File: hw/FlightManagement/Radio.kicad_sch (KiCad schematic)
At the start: 41 parts, among them J1 BWSMA-KE-Z001, U6 XA17-G4K, Y1 13.56 MHz, Y2 10.7 MHz, Y3 6.6128 MHz

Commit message: add pdf outputs
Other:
- company: (none) -> Daniel Enrique Pérez Díaz (steewBSD)
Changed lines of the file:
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@@
 	(generator_version "9.0")
 	(paper "A4")
+	(title_block
+		(company "Daniel Enrique Pérez Díaz (steewBSD)")
+	)
 	(text_box "Receiver\n(433 MHz Vertical)"
 		(exclude_from_sim no)

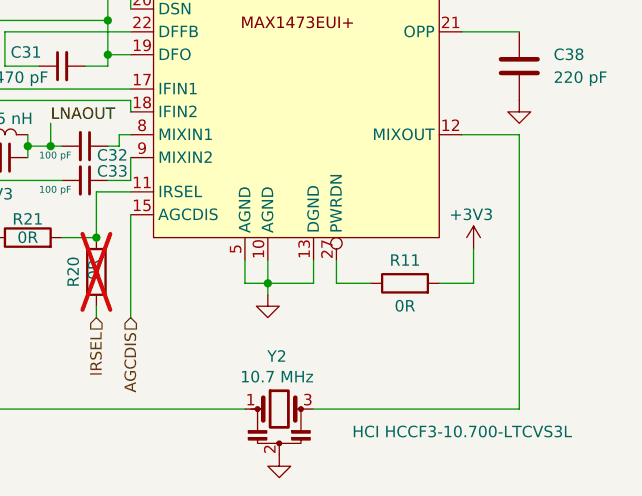
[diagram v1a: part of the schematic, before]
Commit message: add NOR flash in FC
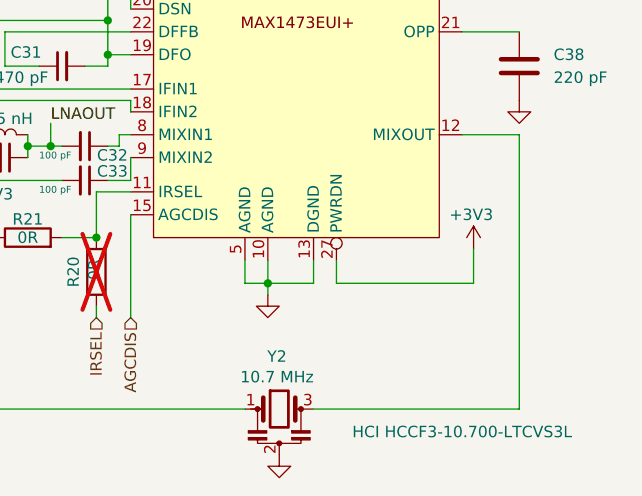
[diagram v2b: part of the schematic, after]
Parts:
- removed R11: 0R, Resistor_SMD:R_0603_1608Metric_Pad0.98x0.95mm_HandSolder, symbol Device:R
- C17, C18, C19, C20, C21, C22, C23, C24, C25, C26, C27, C28, C29, C30, C31, C32, C33, C34, C35, C36, C37, C38, C47: footprint Capacitor_SMD:C_0805_2012Metric_Pad1.18x1.45mm_HandSolder -> Capacitor_SMD:C_0603_1608Metric_Pad1.08x0.95mm_HandSolder
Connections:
- net +3V3: now also U7.27 (PWRDN)
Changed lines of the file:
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@@
 	(wire
 		(pts
-			(xy 226.06 119.38) (xy 222.25 119.38)
-		)
-		(stroke
-			(width 0)
-			(type default)
-		)
-	)
-	(wire
-		(pts
 			(xy 185.42 86.36) (xy 185.42 90.17)
 		)
@@
 	(wire
 		(pts
-			(xy 210.82 119.38) (xy 214.63 119.38)
+			(xy 210.82 119.38) (xy 226.06 119.38)
 		)
 		(stroke
@@
 			)
 		)
-		(property "Footprint" "Capacitor_SMD:C_0805_2012Metric_Pad1.18x1.45mm_HandSolder"
+		(property "Footprint" "Capacitor_SMD:C_0603_1608Metric_Pad1.08x0.95mm_HandSolder"
 			(at 167.64 80.01 0)
 			(effects
@@
 			)
 		)
-		(property "Footprint" "Capacitor_SMD:C_0805_2012Metric_Pad1.18x1.45mm_HandSolder"
+		(property "Footprint" "Capacitor_SMD:C_0603_1608Metric_Pad1.08x0.95mm_HandSolder"
 			(at 232.1052 99.06 0)
 			(effects
@@
 			)
 		)
-		(property "Footprint" "Capacitor_SMD:C_0805_2012Metric_Pad1.18x1.45mm_HandSolder"
+		(property "Footprint" "Capacitor_SMD:C_0603_1608Metric_Pad1.08x0.95mm_HandSolder"
 			(at 106.68 73.66 0)
 			(effects
@@
 	)
 	(symbol
-		(lib_id "Device:R")
-		(at 218.44 119.38 90)
-		(unit 1)
-		(exclude_from_sim no)
-		(in_bom yes)
-		(on_board yes)
-		(dnp no)
-		(property "Reference" "R11"
-			(at 218.44 116.84 90)
-			(effects
-				(font
-					(size 1.27 1.27)
-				)
-			)
-		)
-		(property "Value" "0R"
-			(at 218.44 121.92 90)
-			(effects
-				(font
-					(size 1.27 1.27)
-				)
-			)
-		)
-		(property "Footprint" "Resistor_SMD:R_0603_1608Metric_Pad0.98x0.95mm_HandSolder"
-			(at 218.44 121.158 90)
-			(effects
-				(font
-					(size 1.27 1.27)
-				)
-				(hide yes)
-			)
-		)
-		(property "Datasheet" "~"
-			(at 218.44 119.38 0)
-			(effects
-				(font
-					(size 1.27 1.27)
-				)
-				(hide yes)
-			)
-		)
-		(property "Description" "Resistor"
-			(at 218.44 119.38 0)
-			(effects
-				(font
-					(size 1.27 1.27)
-				)
-				(hide yes)
-			)
-		)
-		(pin "2"
-		)
-		(pin "1"
-		)
-		(instances
-			(project "FlightManagement"
-				(path "/428dbf80-1251-4f56-8786-11b9f3c75d18/59439b12-3d5b-4d3f-87cb-66bd691f4bfb"
-					(reference "R11")
-					(unit 1)
-				)
-			)
-		)
-	)
-	(symbol
 		(lib_id "Device:C_Small")
 		(at 165.1 111.76 180)
@@
 			)
 		)
-		(property "Footprint" "Capacitor_SMD:C_0805_2012Metric_Pad1.18x1.45mm_HandSolder"
+		(property "Footprint" "Capacitor_SMD:C_0603_1608Metric_Pad1.08x0.95mm_HandSolder"
 			(at 165.1 111.76 0)
 			(effects
@@
 			)
 		)
-		(property "Footprint" "Capacitor_SMD:C_0805_2012Metric_Pad1.18x1.45mm_HandSolder"
+		(property "Footprint" "Capacitor_SMD:C_0603_1608Metric_Pad1.08x0.95mm_HandSolder"
 			(at 78.74 76.2 0)
 			(effects
@@
 			)
 		)
-		(property "Footprint" "Capacitor_SMD:C_0805_2012Metric_Pad1.18x1.45mm_HandSolder"
+		(property "Footprint" "Capacitor_SMD:C_0603_1608Metric_Pad1.08x0.95mm_HandSolder"
 			(at 154.94 64.77 0)
 			(effects
@@
 			)
 		)
-		(property "Footprint" "Capacitor_SMD:C_0805_2012Metric_Pad1.18x1.45mm_HandSolder"
+		(property "Footprint" "Capacitor_SMD:C_0603_1608Metric_Pad1.08x0.95mm_HandSolder"
 			(at 198.12 57.15 0)
 			(effects
@@
 			)
 		)
-		(property "Footprint" "Capacitor_SMD:C_0805_2012Metric_Pad1.18x1.45mm_HandSolder"
+		(property "Footprint" "Capacitor_SMD:C_0603_1608Metric_Pad1.08x0.95mm_HandSolder"
 			(at 125.73 62.23 0)
 			(effects
@@
 			)
 		)
-		(property "Footprint" "Capacitor_SMD:C_0805_2012Metric_Pad1.18x1.45mm_HandSolder"
+		(property "Footprint" "Capacitor_SMD:C_0603_1608Metric_Pad1.08x0.95mm_HandSolder"
 			(at 173.99 105.41 0)
 			(effects
@@
 			)
 		)
-		(property "Footprint" "Capacitor_SMD:C_0805_2012Metric_Pad1.18x1.45mm_HandSolder"
+		(property "Footprint" "Capacitor_SMD:C_0603_1608Metric_Pad1.08x0.95mm_HandSolder"
 			(at 124.46 86.36 0)
 			(effects
@@
 			)
 		)
-		(property "Footprint" "Capacitor_SMD:C_0805_2012Metric_Pad1.18x1.45mm_HandSolder"
+		(property "Footprint" "Capacitor_SMD:C_0603_1608Metric_Pad1.08x0.95mm_HandSolder"
 			(at 212.09 57.15 0)
 			(effects
@@
 			)
 		)
-		(property "Footprint" "Capacitor_SMD:C_0805_2012Metric_Pad1.18x1.45mm_HandSolder"
+		(property "Footprint" "Capacitor_SMD:C_0603_1608Metric_Pad1.08x0.95mm_HandSolder"
 			(at 217.17 57.15 0)
 			(effects
@@
 			)
 		)
-		(property "Footprint" "Capacitor_SMD:C_0805_2012Metric_Pad1.18x1.45mm_HandSolder"
+		(property "Footprint" "Capacitor_SMD:C_0603_1608Metric_Pad1.08x0.95mm_HandSolder"
 			(at 182.88 107.95 0)
 			(effects
@@
 			)
 		)
-		(property "Footprint" "Capacitor_SMD:C_0805_2012Metric_Pad1.18x1.45mm_HandSolder"
+		(property "Footprint" "Capacitor_SMD:C_0603_1608Metric_Pad1.08x0.95mm_HandSolder"
 			(at 182.88 104.14 0)
 			(effects
@@
 			)
 		)
-		(property "Footprint" "Capacitor_SMD:C_0805_2012Metric_Pad1.18x1.45mm_HandSolder"
+		(property "Footprint" "Capacitor_SMD:C_0603_1608Metric_Pad1.08x0.95mm_HandSolder"
 			(at 154.94 59.69 0)
 			(effects
@@
 			)
 		)
-		(property "Footprint" "Capacitor_SMD:C_0805_2012Metric_Pad1.18x1.45mm_HandSolder"
+		(property "Footprint" "Capacitor_SMD:C_0603_1608Metric_Pad1.08x0.95mm_HandSolder"
 			(at 205.74 57.15 0)
 			(effects
@@
 			)
 		)
-		(property "Footprint" "Capacitor_SMD:C_0805_2012Metric_Pad1.18x1.45mm_HandSolder"
+		(property "Footprint" "Capacitor_SMD:C_0603_1608Metric_Pad1.08x0.95mm_HandSolder"
 			(at 180.34 95.25 0)
 			(effects
@@
 			)
 		)
-		(property "Footprint" "Capacitor_SMD:C_0805_2012Metric_Pad1.18x1.45mm_HandSolder"
+		(property "Footprint" "Capacitor_SMD:C_0603_1608Metric_Pad1.08x0.95mm_HandSolder"
 			(at 109.22 86.36 0)
 			(effects
@@
 			)
 		)
-		(property "Footprint" "Capacitor_SMD:C_0805_2012Metric_Pad1.18x1.45mm_HandSolder"
+		(property "Footprint" "Capacitor_SMD:C_0603_1608Metric_Pad1.08x0.95mm_HandSolder"
 			(at 113.03 73.66 0)
 			(effects
@@
 			)
 		)
-		(property "Footprint" "Capacitor_SMD:C_0805_2012Metric_Pad1.18x1.45mm_HandSolder"
+		(property "Footprint" "Capacitor_SMD:C_0603_1608Metric_Pad1.08x0.95mm_HandSolder"
 			(at 100.33 73.66 0)
 			(effects
@@
 			)
 		)
-		(property "Footprint" "Capacitor_SMD:C_0805_2012Metric_Pad1.18x1.45mm_HandSolder"
+		(property "Footprint" "Capacitor_SMD:C_0603_1608Metric_Pad1.08x0.95mm_HandSolder"
 			(at 150.8252 109.22 0)
 			(effects
@@
 			)
 		)
-		(property "Footprint" "Capacitor_SMD:C_0805_2012Metric_Pad1.18x1.45mm_HandSolder"
+		(property "Footprint" "Capacitor_SMD:C_0603_1608Metric_Pad1.08x0.95mm_HandSolder"
 			(at 100.33 82.55 0)
 			(effects
@@
 			)
 		)
-		(property "Footprint" "Capacitor_SMD:C_0805_2012Metric_Pad1.18x1.45mm_HandSolder"
+		(property "Footprint" "Capacitor_SMD:C_0603_1608Metric_Pad1.08x0.95mm_HandSolder"
 			(at 155.9052 109.22 0)
 			(effects

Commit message: FMU completed
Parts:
- renumbered C22 to C14, C31 to C21, C33 to C23, C47 to C26, C37 to C27, C29 to C28, C23 to C29, C21 to C30, C18 to C31, C25 to C32, C24 to C33, C26 to C34, C38 to C35, C19 to C36, C17 to C37, C28 to C38, C36 to C39, C35 to C40, C34 to C41, C30 to C51, C32 to C52, C27 to C7, C20 to C9, J1 to J4, L1 to L3, L2 to L4, L4 to L5, L3 to L6, L5 to L7, R21 to R10, R20 to R14, R17 to R16, R16 to R17, R10 to R18, U6 to U5, U5 to U6, U7 to U8, Y3 to Y2, Y2 to Y3, Y1 to Y4

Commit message: start working on firmware
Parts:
- renumbered C7 to C13, C14 to C18, C23 to C21, C21 to C23, C31 to C26, C26 to C27, C27 to C28, C28 to C29, C29 to C30, C30 to C31, C41 to C38, C40 to C39, C39 to C40, C38 to C41, C52 to C49, C51 to C50, C9 to C7, R14 to R11, R10 to R13, R18 to R16, R16 to R18
